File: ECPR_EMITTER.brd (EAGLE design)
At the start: 66 x 95 mm, 17 parts, among them IC1 78L05, IC2 ATMEGA8-PU, J1 0802_SCREEN, Q1 BFR96, U1 AD9850 DDS Module

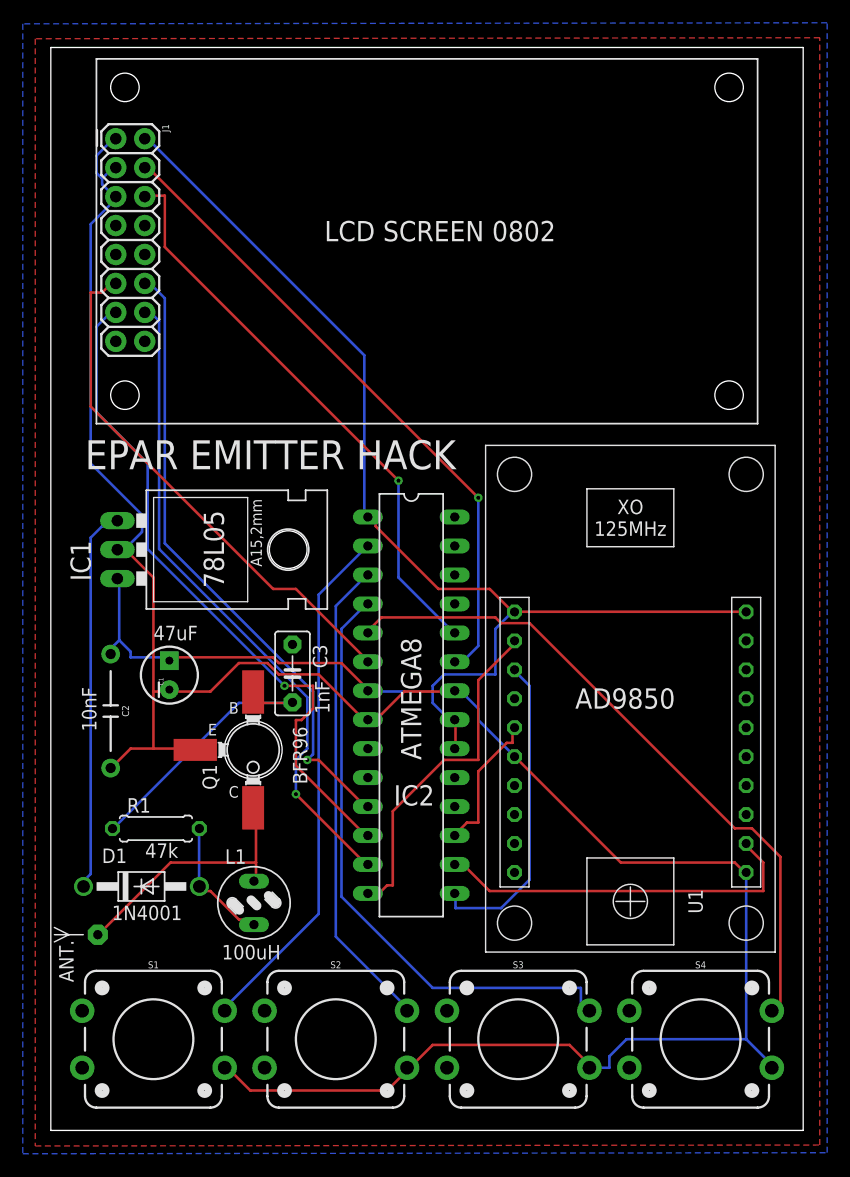
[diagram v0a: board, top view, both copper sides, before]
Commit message: feat(board): final version w/ led, switch, pads for battery, rf connected, new version of AD9850 libs
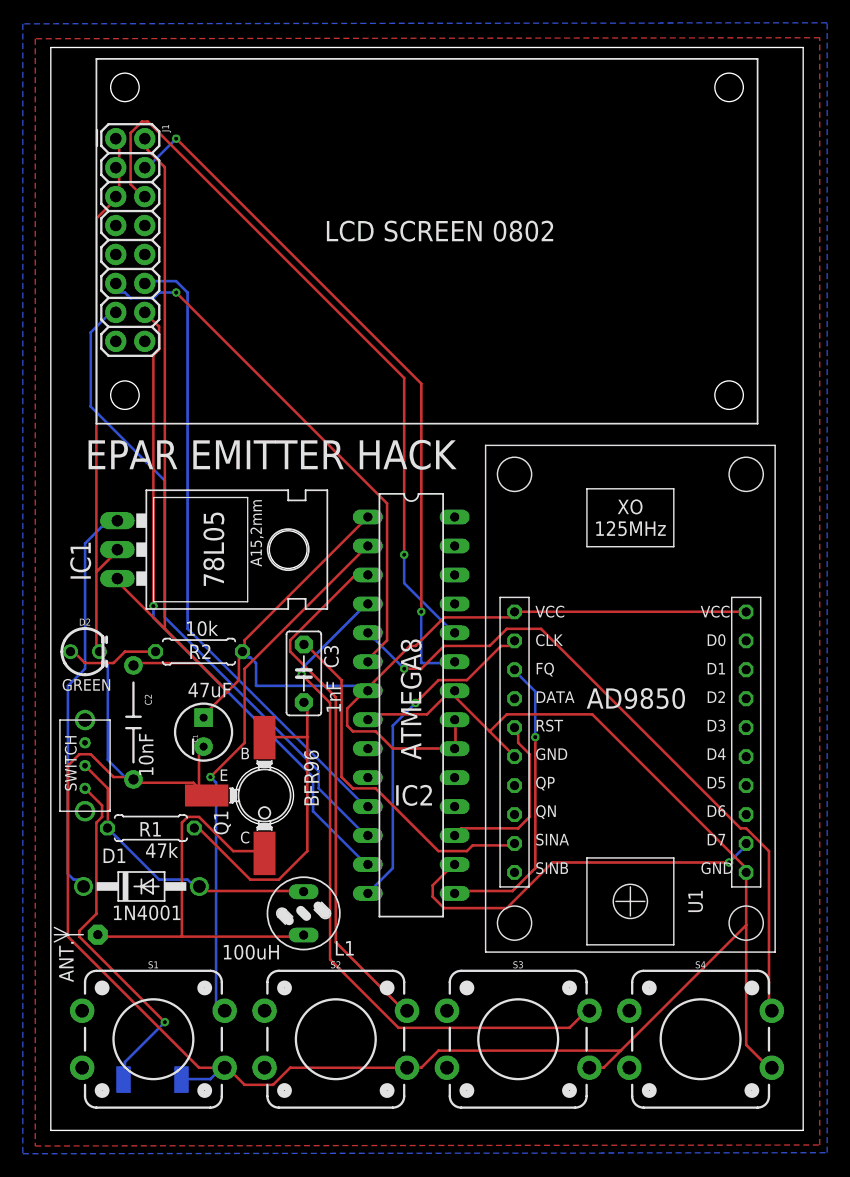
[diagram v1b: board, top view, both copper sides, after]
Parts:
- added D2: GREEN, SparkFun-LED:LED_3MM-NS
- added R2: 10k, resistor:0207/7
- added U$2: PACKAGESWITCH, SLIDESWITCH:SLIDESWITCH
- added U$3: BAT, BATTERY:BAT
- moved C1 5.83 mm to (13.4, 34.9)
- moved L1 4.46 mm to (22.2, 19.0), turned to 180 degrees
- moved Q1 4.12 mm to (18.8, 29.4)
- moved C2 2.24 mm to (7.25, 35.8)
- moved C3 1.00 mm to (22.2, 40.1)
- moved R1 0.44 mm to (8.78, 26.5), turned to 180 degrees
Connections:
- new net N$16: D2.A, R2.1
- net D7: now also U1.D7; no longer U1.2
- net FQ_UD: now also U1.FQ; no longer U1.13
- net GND: now also D2.K, U$3.-, U1.GND, U1.GND0; no longer U1.1, U1.16
- net N$12: now also U$2.P$3, U$3.+; no longer IC2.12
- net N$13: now also IC2.12
- net RESET: now also U1.RST; no longer U1.15
- net RF: now also U1.SINA
- net VBAT: now also U$2.P$2
- net VCC: now also R2.2, U1.VCC, U1.VCC0; no longer U1.10, U1.11
- net W_CLK: now also U1.CLK; no longer U1.12
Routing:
- net GND: track 205.2 -> 238.7 mm
- net N$12: track 0.00 -> 31.6 mm, vias 0 -> 1
- net RF: track 0.00 -> 31.2 mm
- net VCC: track 134.3 -> 154.5 mm
- net VBAT: track 11.3 -> 26.3 mm
- net N$7: track 23.1 -> 36.9 mm
- net N$9: track 50.7 -> 64.1 mm
- net N$16: track 0.00 -> 8.29 mm
- net N$5: track 53.5 -> 60.5 mm, vias 0 -> 1
- net N$2: track 24.3 -> 29.9 mm
- net N$8: track 57.4 -> 61.9 mm, vias 1 -> 2
- net N$4: track 42.2 -> 46.1 mm
- net RESET: track 12.5 -> 15.6 mm
- net N$13: track 59.7 -> 57.4 mm, vias 1 -> 0
- net FQ_UD: track 27.8 -> 26.2 mm, vias 0 -> 1
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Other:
- board text added: "10k"
- board text added: "CLK"
- board text added: "D0"
- board text added: "D1"
- board text added: "D2"
- board text added: "D3"
- board text added: "D4"
- board text added: "D5"
- board text added: "D6"
- board text added: "D7"
- board text added: "DATA"
- board text added: "FQ"
- board text added: "GND"
- board text added: "GREEN"
- board text added: "QN"
- board text added: "QP"
- board text added: "RST"
- board text added: "SINA"
- board text added: "SINB"
- board text added: "SWITCH"
- board text added: "VCC"

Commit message: feat(button): move button to the top
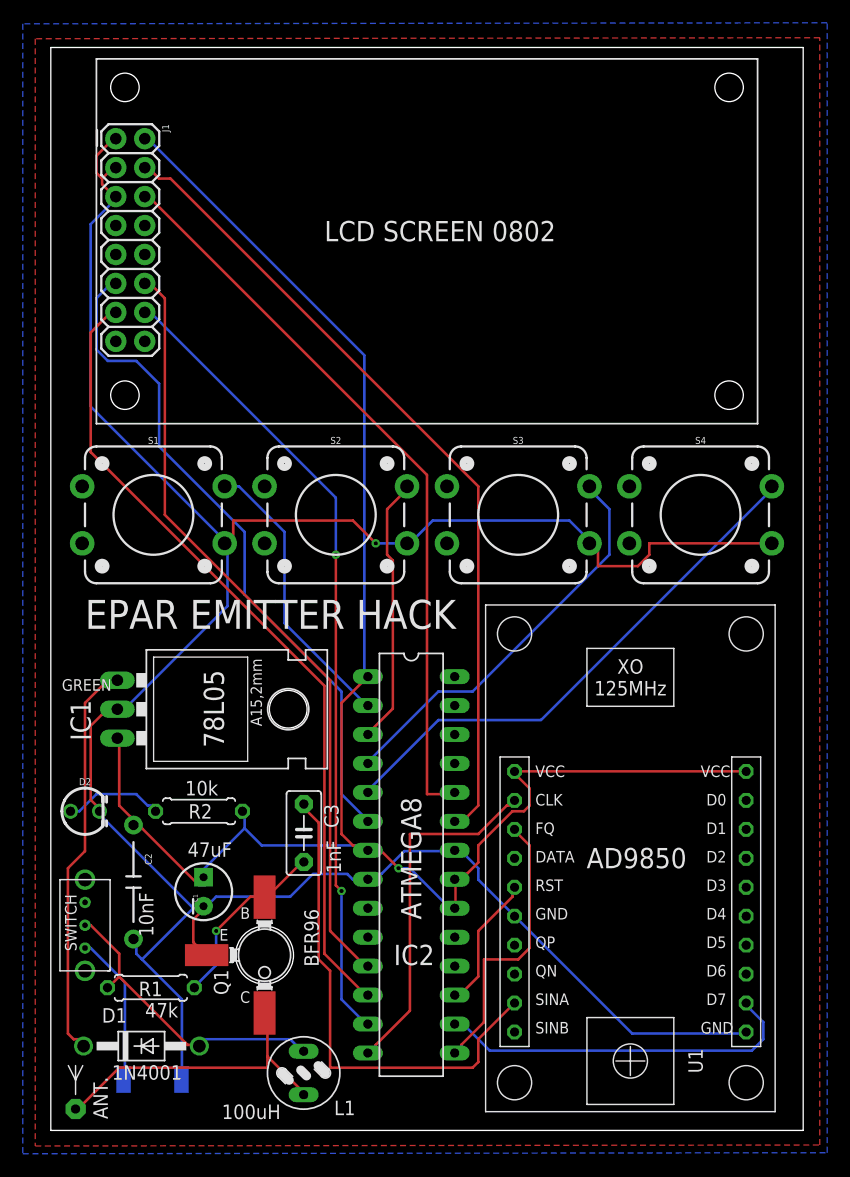
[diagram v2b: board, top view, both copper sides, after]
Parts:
- moved S1 46.0 mm to (9.00, 54.0)
- moved S2 46.0 mm to (25.0, 54.0)
- moved S3 46.0 mm to (41.0, 54.0)
- moved S4 46.0 mm to (57.0, 54.0)
- moved U$1 15.4 mm to (2.17, 1.88), turned to 0 degrees
- moved C3 14.0 mm to (22.2, 26.1)
- moved C2 14.0 mm to (7.25, 21.8)
- moved D2 14.0 mm to (3.00, 28.0)
- moved IC1 14.0 mm to (9.65, 37.0)
- moved L1 14.0 mm to (22.2, 5.04)
- moved R1 14.0 mm to (8.78, 12.5)
- moved R2 14.0 mm to (13.0, 28.0)
- moved U$2 14.0 mm to (3.00, 20.0)
- moved D1 14.0 mm to (7.95, 7.40)
- moved Q1 14.0 mm to (18.8, 15.4)
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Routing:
- net N$5: track 60.5 -> 35.9 mm, vias 1 -> 0
- net N$4: track 46.1 -> 23.7 mm
- net N$3: track 47.2 -> 25.2 mm, vias 1 -> 0
- net N$12: track 31.6 -> 13.4 mm, vias 1 -> 0
- net N$10: track 57.0 -> 71.1 mm, vias 1 -> 2
- net N$13: track 57.4 -> 71.4 mm
- net N$2: track 29.9 -> 16.0 mm, vias 0 -> 1
- net N$6: track 60.3 -> 47.1 mm, vias 1 -> 0
- net RF: track 31.2 -> 43.9 mm
- net N$11: track 56.0 -> 68.5 mm
- net N$14: track 47.5 -> 59.6 mm, vias 1 -> 0
- net GND: track 238.7 -> 228.1 mm, vias 0 -> 1
- net N$8: track 61.9 -> 72.0 mm, vias 2 -> 0
- net N$7: track 36.9 -> 27.8 mm
- net RESET: track 15.6 -> 12.3 mm
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
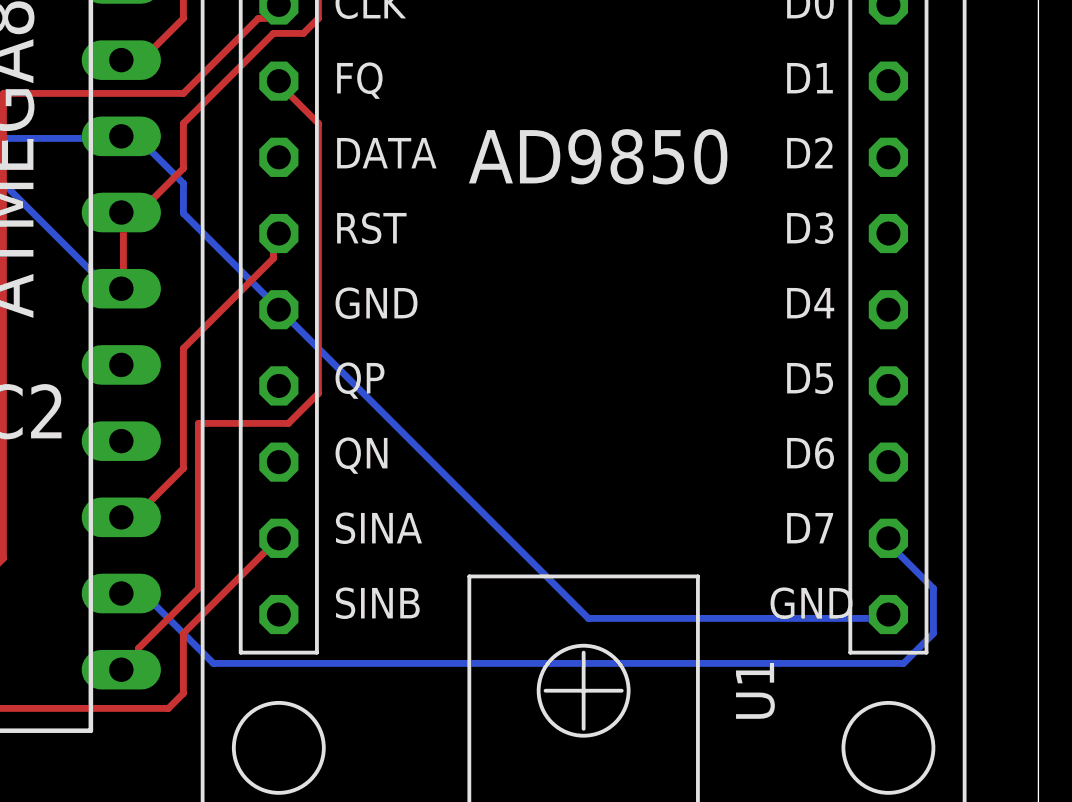
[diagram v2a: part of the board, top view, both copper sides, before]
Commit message: feat(testpin): add rf out and update to eagle 9.4.0
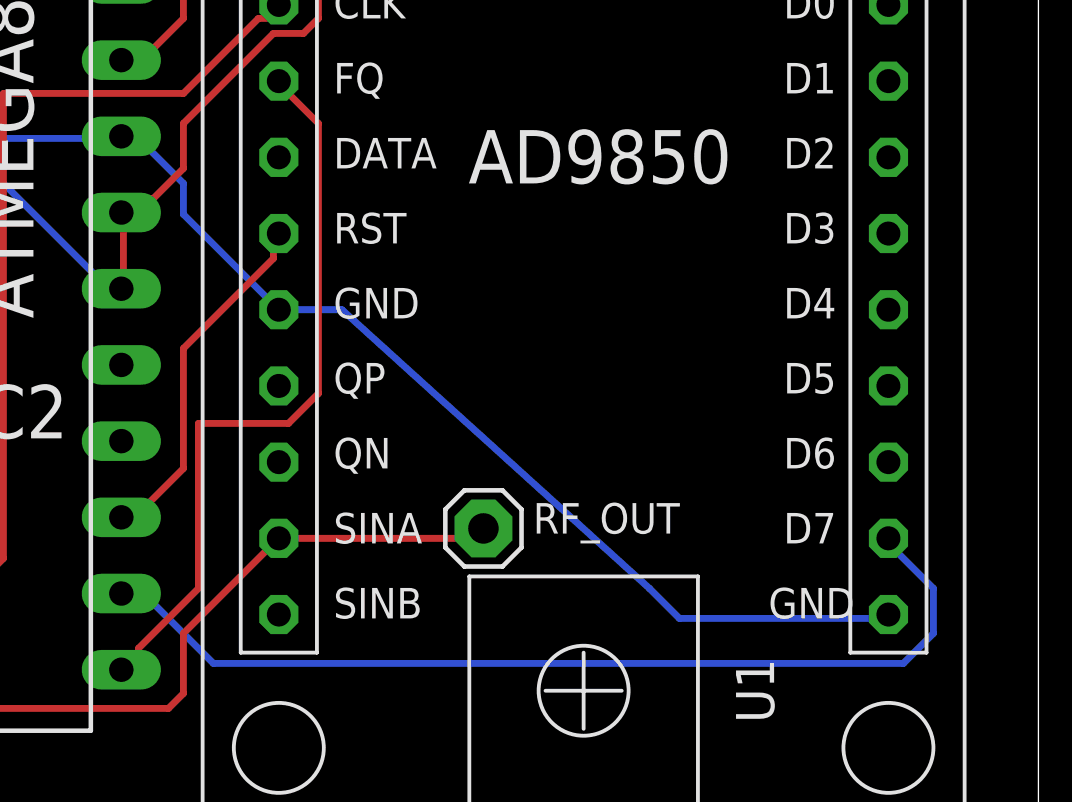
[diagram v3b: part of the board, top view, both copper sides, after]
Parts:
- added RF_OUT: (no value), adafruit:1X01
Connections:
- net RF: now also RF_OUT.1
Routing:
- net RF: track 43.9 -> 50.8 mm
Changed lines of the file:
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@@
 <?xml version="1.0" encoding="utf-8"?>
 <!DOCTYPE eagle SYSTEM "eagle.dtd">
-<eagle version="9.3.2">
+<eagle version="9.4.0">
 <drawing>
 <settings>
@@
 <element name="U$2" library="SLIDESWITCH" package="SLIDESWITCH" value="PACKAGESWITCH" x="3" y="20" smashed="yes"/>
 <element name="U$3" library="BATTERY" package="BAT" value="BAT" x="14" y="7" smashed="yes" rot="MR0"/>
+<element name="RF_OUT" library="adafruit" package="1X01" value="" x="47.5" y="11.5" smashed="yes">
+<attribute name="NAME" x="49.1538" y="11.3288" size="1.016" layer="25" ratio="10"/>
+<attribute name="VALUE" x="46.23" y="8.325" size="1.27" layer="27"/>
+</element>
 </elements>
 <signals>
@@
 <wire x1="40.5" y1="11" x2="40.68" y2="11.17" width="0.2286" layer="1"/>
 <wire x1="22.5" y1="28.5" x2="22.2" y2="28.63" width="0.2286" layer="1"/>
+<contactref element="RF_OUT" pad="1"/>
+<wire x1="47.5" y1="11.5" x2="47.17" y2="11.17" width="0.2286" layer="1"/>
+<wire x1="47.17" y1="11.17" x2="40.68" y2="11.17" width="0.2286" layer="1"/>
 </signal>
 <signal name="D7">
@@
 <contactref element="D2" pad="K"/>
 <contactref element="U$3" pad="-"/>
-<wire x1="37.5" y1="22" x2="40.5" y2="19" width="0.2286" layer="16"/>
-<wire x1="37.5" y1="23" x2="37.5" y2="22" width="0.2286" layer="16"/>
+<wire x1="37.5" y1="23" x2="37.5" y2="21.97" width="0.2286" layer="16"/>
 <wire x1="35.5" y1="25" x2="37.5" y2="23" width="0.2286" layer="16"/>
-<wire x1="40.5" y1="19" x2="40.68" y2="18.79" width="0.2286" layer="16"/>
+<wire x1="37.5" y1="21.97" x2="40.68" y2="18.79" width="0.2286" layer="16"/>
 <wire x1="35.5" y1="25" x2="35.43" y2="24.57" width="0.2286" layer="16"/>
-<wire x1="51" y1="8.5" x2="61" y2="8.5" width="0.2286" layer="16"/>
-<wire x1="41" y1="18.5" x2="51" y2="8.5" width="0.2286" layer="16"/>
+<wire x1="54.03448125" y1="8.5" x2="61" y2="8.5" width="0.2286" layer="16"/>
+<wire x1="53.034465625" y1="9.500015625" x2="54.03448125" y2="8.5" width="0.2286" layer="16"/>
 <wire x1="61" y1="8.5" x2="61" y2="8.63" width="0.2286" layer="16"/>
-<wire x1="41" y1="18.5" x2="40.68" y2="18.79" width="0.2286" layer="16"/>
+<wire x1="53.034465625" y1="9.500015625" x2="42.783446875" y2="18.79" width="0.2286" layer="16"/>
+<wire x1="42.783446875" y1="18.79" x2="40.68" y2="18.79" width="0.2286" layer="16"/>
 <wire x1="29" y1="22.5" x2="28" y2="22.5" width="0.2286" layer="16"/>
 <wire x1="31" y1="24.5" x2="29" y2="22.5" width="0.2286" layer="16"/>
